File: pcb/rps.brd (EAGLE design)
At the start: 23.6 x 26 mm, 15 parts, among them SW1 MK-12C02 G1.5, SW2 DHT-4235A, SW3 DHT-4235A, SW4 DHT-4235A, SW5 B3U-1000P-2P-SMD, U1 ATTINY1614-SSNR

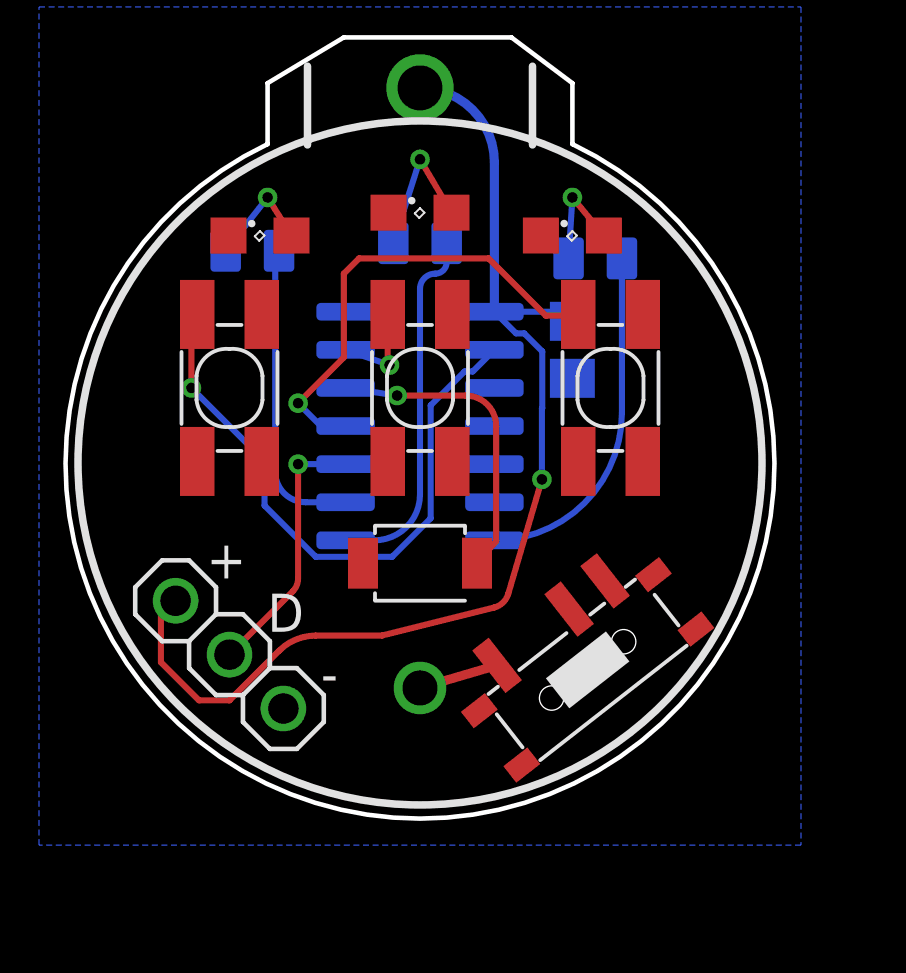
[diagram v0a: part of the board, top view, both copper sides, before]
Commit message: adjusted pad sizes for buttons on PCB
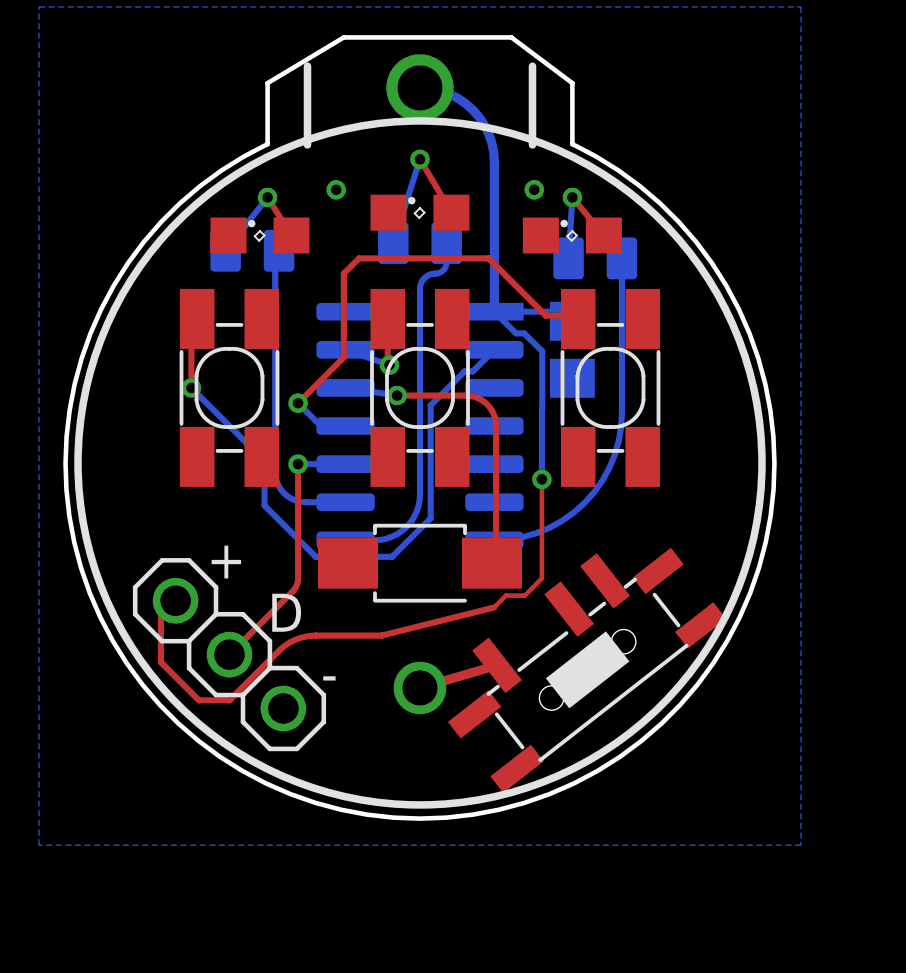
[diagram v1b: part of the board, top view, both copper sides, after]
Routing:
- net VCC: track 37.1 -> 37.7 mm
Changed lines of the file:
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@@
 <?xml version="1.0" encoding="utf-8"?>
 <!DOCTYPE eagle SYSTEM "eagle.dtd">
-<eagle version="9.3.0">
+<eagle version="9.4.2">
 <drawing>
 <settings>
-<setting alwaysvectorfont="no"/>
+<setting alwaysvectorfont="yes"/>
 <setting verticaltext="up"/>
 </settings>
@@
 <contactref element="D2" pad="C"/>
 <contactref element="D3" pad="C"/>
+<via x="12.446" y="23.114" extent="1-16" drill="0.35"/>
+<via x="19.05" y="23.114" extent="1-16" drill="0.35"/>
 </signal>
 <signal name="NEG">
@@
 <via x="19.304" y="13.462" extent="1-16" drill="0.35"/>
 <wire x1="13.97" y1="8.256" x2="17.705515625" y2="9.188409375" width="0.2032" layer="1"/>
-<wire x1="17.705515625" y1="9.188409375" x2="18.181321875" y2="9.644896875" width="0.2032" layer="1" curve="59.595302"/>
-<wire x1="18.181321875" y1="9.644896875" x2="19.304" y2="13.462" width="0.2032" layer="1"/>
+<wire x1="17.705515625" y1="9.188409375" x2="18.10650625" y2="9.5894" width="0.1524" layer="1"/>
+<wire x1="18.10650625" y1="9.5894" x2="18.7346875" y2="9.5894" width="0.1524" layer="1"/>
+<wire x1="18.7346875" y1="9.5894" x2="19.304" y2="10.1587125" width="0.1524" layer="1"/>
+<wire x1="19.304" y1="10.1587125" x2="19.304" y2="13.462" width="0.1524" layer="1"/>
 </signal>
 <signal name="N$1">
@@
 <contactref element="SW4" pad="2"/>
 <contactref element="U1" pad="11"/>
-<wire x1="20.48006875" y1="18.917728125" x2="20.515" y2="18.96" width="0.2032" layer="1"/>
+<wire x1="20.48006875" y1="18.917728125" x2="20.515" y2="18.81" width="0.2032" layer="1"/>
 <wire x1="12.76" y1="15.24" x2="11.938" y2="15.24" width="0.2032" layer="16"/>
 <wire x1="11.938" y1="15.24" x2="11.176" y2="16.002" width="0.2032" layer="16"/>
@@
 <contactref element="SW5" pad="2"/>
 <wire x1="17.78" y1="15.24" x2="17.78" y2="11.4016" width="0.2032" layer="1"/>
-<wire x1="17.78" y1="11.4016" x2="17.14" y2="10.668" width="0.2032" layer="1"/>
+<wire x1="17.78" y1="11.4016" x2="17.64" y2="10.668" width="0.2032" layer="1"/>
 </signal>
 <signal name="N$4">
@@
 <via x="14.224" y="17.272" extent="1-16" drill="0.35"/>
 <wire x1="14.224" y1="17.272" x2="14.165" y2="17.272" width="0.2032" layer="1"/>
-<wire x1="14.165" y1="17.272" x2="14.165" y2="18.96" width="0.2032" layer="1"/>
+<wire x1="14.165" y1="17.272" x2="14.165" y2="18.81" width="0.2032" layer="1"/>
 </signal>
 <signal name="N$5">
@@
 <wire x1="10.0584" y1="12.58879375" x2="10.0584" y2="14.0716" width="0.2032" layer="16"/>
 <wire x1="7.62" y1="16.51" x2="7.62" y2="18.265" width="0.2032" layer="1"/>
-<wire x1="7.62" y1="18.265" x2="7.815" y2="18.96" width="0.2032" layer="1"/>
+<wire x1="7.62" y1="18.265" x2="7.815" y2="18.81" width="0.2032" layer="1"/>
 </signal>
 <signal name="N$6">
